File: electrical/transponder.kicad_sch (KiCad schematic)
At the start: 4 parts

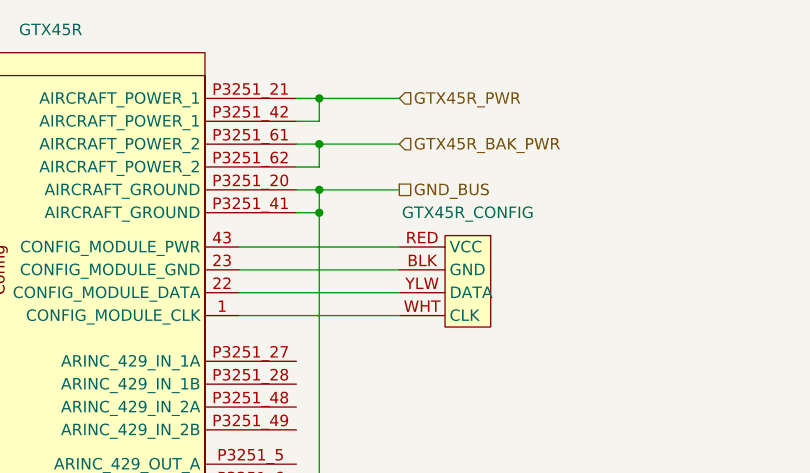
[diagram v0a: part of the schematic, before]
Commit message: Changed grounds and canbuses to be in/out when applicable.
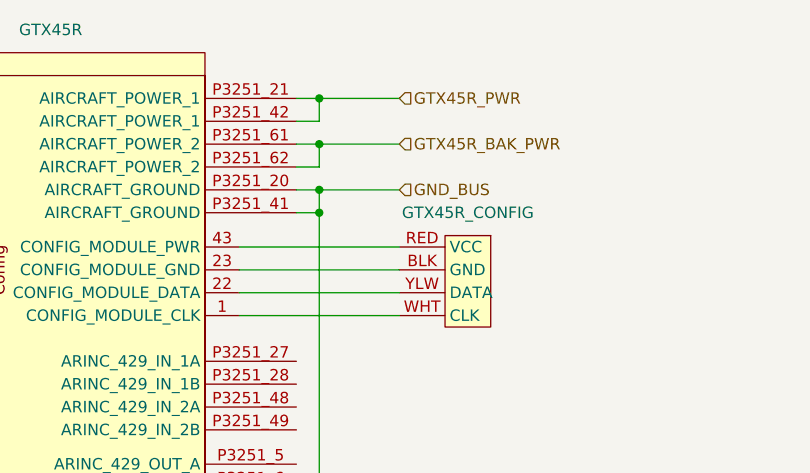
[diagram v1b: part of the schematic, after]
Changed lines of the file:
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@@
     (effects (font (size 1.27 1.27)) (justify left))
   )
-  (hierarchical_label "GND_BUS" (shape passive) (at 88.9 46.99 0) (fields_autoplaced)
+  (hierarchical_label "GND_BUS" (shape input) (at 88.9 46.99 0) (fields_autoplaced)
     (effects (font (size 1.27 1.27)) (justify left))
   )
